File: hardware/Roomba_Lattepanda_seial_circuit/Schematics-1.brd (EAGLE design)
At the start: 32.7 x 25.4 mm, 13 parts

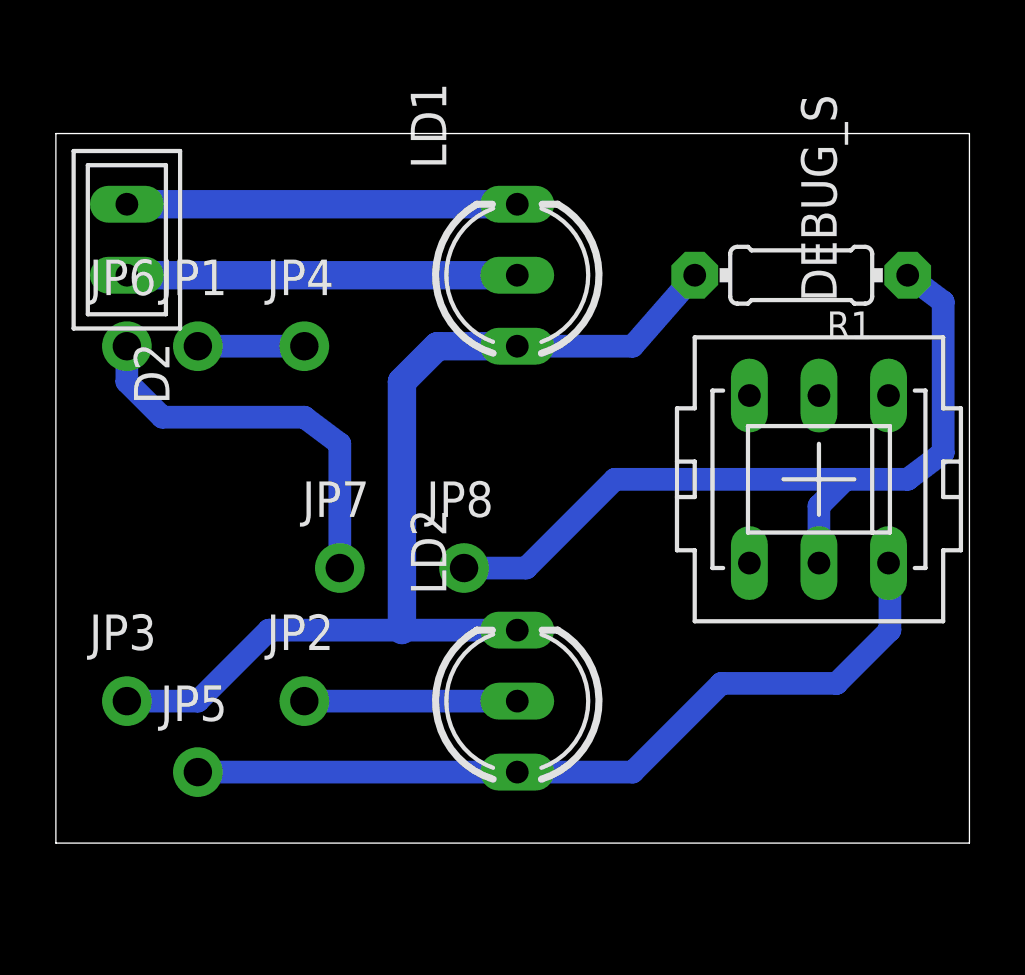
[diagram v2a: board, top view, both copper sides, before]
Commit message: add new concept art to repo + fix the style of media list + toggle augment
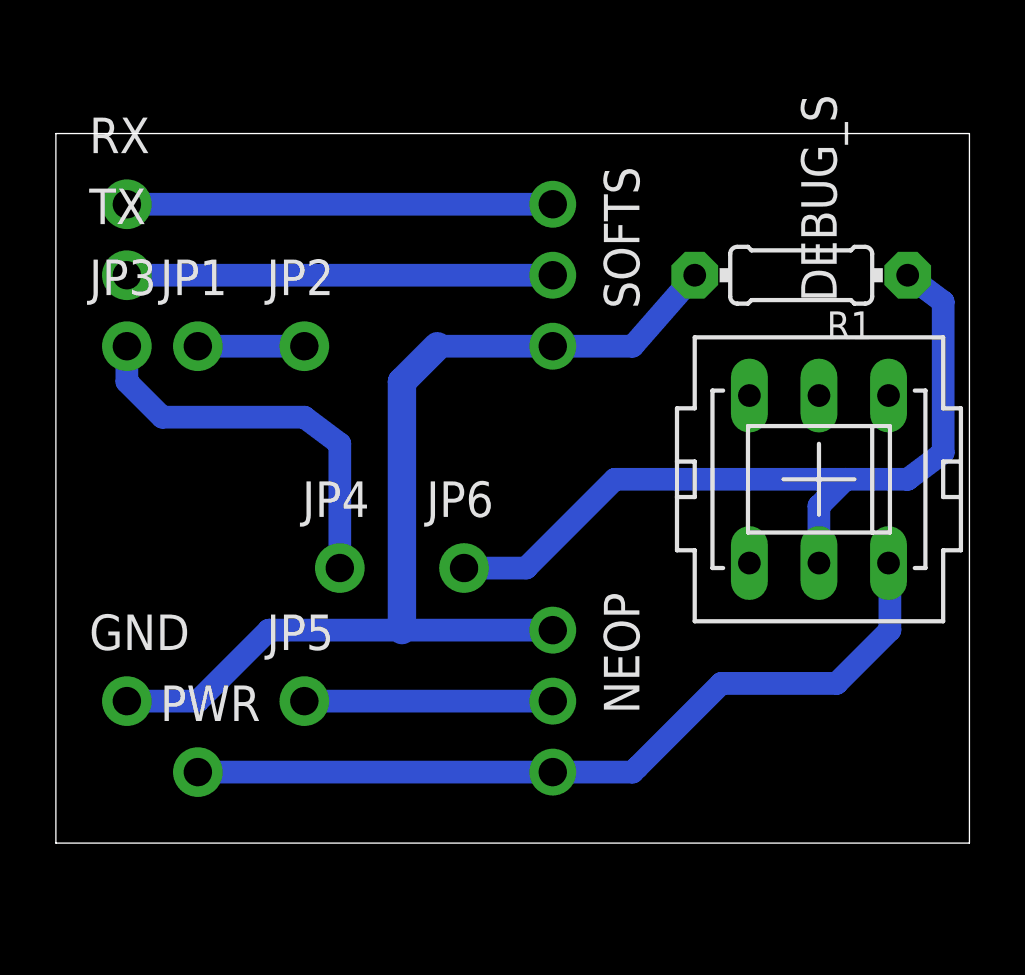
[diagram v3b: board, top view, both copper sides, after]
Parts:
- removed D2: U57X32, led:U57X32
- removed JP7, JP8: (no value), adafruit:1X01-CLEANBIG
- removed LD1, LD2: (no value), led:DUOLED-C-5MM
- added GND, PWR, RX, TX: (no value), adafruit:1X01-CLEANBIG
- added NEOP, SOFTS: (no value), adafruit:1X03-CLEANBIG
- moved JP6 14.4 mm to (14.6, 9.84)
- moved JP2 12.7 mm to (8.89, 17.8)
- moved JP3 12.7 mm to (2.54, 17.8)
- moved JP4 8.04 mm to (10.2, 9.84)
- moved JP5 4.58 mm to (8.89, 5.08)
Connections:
- net N$1: now also RX.1, SOFTS.1; no longer D2.A, LD1.AR
- net N$2: now also JP2.1; no longer JP4.1
- net N$3: now also SOFTS.2, TX.1; no longer D2.K, LD1.C
- net N$4: now also GND.1, NEOP.1, SOFTS.3; no longer JP3.1, LD1.AX, LD2.AR
- net N$5: now also NEOP.3, PWR.1; no longer JP5.1, LD2.AX
- net N$6: now also JP6.1; no longer JP8.1
- net N$7: now also JP5.1, NEOP.2; no longer JP2.1, LD2.C
- net N$8: now also JP3.1, JP4.1; no longer JP6.1, JP7.1
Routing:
- net N$7: track 7.62 -> 8.89 mm
- net N$3: track 14.0 -> 15.2 mm
- net N$1: track 14.0 -> 15.2 mm
- net N$4: track 36.1 -> 37.3 mm
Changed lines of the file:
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@@
 </autorouter>
 <elements>
-<element name="LD1" library="led" package="DUOLED-C-5MM" value="" x="16.51" y="20.32" rot="R90"/>
-<element name="D2" library="led" package="U57X32" value="U57X32" x="2.54" y="21.59" rot="R270"/>
 <element name="JP1" library="adafruit" package="1X01-CLEANBIG" value="" x="5.08" y="17.78"/>
-<element name="LD2" library="led" package="DUOLED-C-5MM" value="" x="16.51" y="5.08" rot="R90"/>
-<element name="JP2" library="adafruit" package="1X01-CLEANBIG" value="" x="8.89" y="5.08"/>
-<element name="JP4" library="adafruit" package="1X01-CLEANBIG" value="" x="8.89" y="17.78"/>
-<element name="JP3" library="adafruit" package="1X01-CLEANBIG" value="" x="2.54" y="5.08"/>
-<element name="JP5" library="adafruit" package="1X01-CLEANBIG" value="" x="5.08" y="2.54"/>
+<element name="JP5" library="adafruit" package="1X01-CLEANBIG" value="" x="8.89" y="5.08"/>
+<element name="JP2" library="adafruit" package="1X01-CLEANBIG" value="" x="8.89" y="17.78"/>
+<element name="GND" library="adafruit" package="1X01-CLEANBIG" value="" x="2.54" y="5.08"/>
+<element name="PWR" library="adafruit" package="1X01-CLEANBIG" value="" x="5.08" y="2.54"/>
 <element name="R1" library="adafruit" package="0204/7" value="" x="26.67" y="20.32" rot="R180"/>
 <element name="DEBUG_S" library="switch-misc" package="PVA2R" value="PVA2R" x="27.305" y="13.0175" rot="R90"/>
-<element name="JP6" library="adafruit" package="1X01-CLEANBIG" value="" x="2.54" y="17.78"/>
-<element name="JP7" library="adafruit" package="1X01-CLEANBIG" value="" x="10.16" y="9.8425"/>
-<element name="JP8" library="adafruit" package="1X01-CLEANBIG" value="" x="14.605" y="9.8425"/>
+<element name="JP3" library="adafruit" package="1X01-CLEANBIG" value="" x="2.54" y="17.78"/>
+<element name="JP4" library="adafruit" package="1X01-CLEANBIG" value="" x="10.16" y="9.8425"/>
+<element name="JP6" library="adafruit" package="1X01-CLEANBIG" value="" x="14.605" y="9.8425"/>
+<element name="NEOP" library="adafruit" package="1X03-CLEANBIG" value="" x="17.78" y="5.08" rot="R270"/>
+<element name="SOFTS" library="adafruit" package="1X03-CLEANBIG" value="" x="17.78" y="20.32" rot="R270"/>
+<element name="RX" library="adafruit" package="1X01-CLEANBIG" value="" x="2.54" y="22.86"/>
+<element name="TX" library="adafruit" package="1X01-CLEANBIG" value="" x="2.54" y="20.32"/>
 </elements>
 <signals>
 <signal name="N$4">
-<contactref element="LD1" pad="AX"/>
 <wire x1="12.3825" y1="7.62" x2="12.3825" y2="16.51" width="1.016" layer="16"/>
 <wire x1="12.3825" y1="16.51" x2="13.6525" y2="17.78" width="1.016" layer="16"/>
-<wire x1="13.6525" y1="17.78" x2="16.51" y2="17.78" width="1.016" layer="16"/>
-<contactref element="LD2" pad="AR"/>
-<wire x1="16.51" y1="7.62" x2="12.3825" y2="7.62" width="0.8128" layer="16"/>
 <wire x1="12.3825" y1="7.62" x2="7.62" y2="7.62" width="0.8128" layer="16"/>
 <wire x1="7.62" y1="7.62" x2="5.08" y2="5.08" width="0.8128" layer="16"/>
-<contactref element="JP3" pad="1"/>
+<contactref element="GND" pad="1"/>
 <wire x1="2.54" y1="5.08" x2="5.08" y2="5.08" width="0.8128" layer="16"/>
 <contactref element="R1" pad="2"/>
-<wire x1="16.51" y1="17.78" x2="20.6375" y2="17.78" width="0.8128" layer="16"/>
 <wire x1="20.6375" y1="17.78" x2="22.86" y2="20.32" width="0.8128" layer="16"/>
+<contactref element="SOFTS" pad="3"/>
+<contactref element="NEOP" pad="1"/>
+<wire x1="20.6375" y1="17.78" x2="18.0975" y2="17.78" width="0.8128" layer="16"/>
+<wire x1="17.78" y1="17.78" x2="13.6525" y2="17.78" width="0.8128" layer="16"/>
+<wire x1="17.78" y1="7.62" x2="12.3825" y2="7.62" width="0.8128" layer="16"/>
+<wire x1="17.78" y1="17.78" x2="18.0975" y2="17.78" width="0.8128" layer="16"/>
 </signal>
 <signal name="N$1">
-<contactref element="D2" pad="A"/>
-<contactref element="LD1" pad="AR"/>
-<wire x1="2.54" y1="22.86" x2="16.51" y2="22.86" width="1.016" layer="16"/>
+<contactref element="SOFTS" pad="1"/>
+<contactref element="RX" pad="1"/>
+<wire x1="2.54" y1="22.86" x2="17.78" y2="22.86" width="0.8128" layer="16"/>
 </signal>
 <signal name="N$3">
-<contactref element="D2" pad="K"/>
-<contactref element="LD1" pad="C"/>
-<wire x1="2.54" y1="20.32" x2="16.51" y2="20.32" width="1.016" layer="16"/>
+<contactref element="SOFTS" pad="2"/>
+<contactref element="TX" pad="1"/>
+<wire x1="2.54" y1="20.32" x2="17.78" y2="20.32" width="0.8128" layer="16"/>
 </signal>
 <signal name="N$5">
-<contactref element="LD2" pad="AX"/>
-<contactref element="JP5" pad="1"/>
-<wire x1="5.08" y1="2.54" x2="16.51" y2="2.54" width="0.8128" layer="16"/>
-<wire x1="16.51" y1="2.54" x2="20.6375" y2="2.54" width="0.8128" layer="16"/>
+<contactref element="PWR" pad="1"/>
 <contactref element="DEBUG_S" pad="3"/>
-<wire x1="20.6375" y1="2.54" x2="23.8125" y2="5.715" width="0.8128" layer="16"/>
+<wire x1="20.79625" y1="2.69875" x2="23.8125" y2="5.715" width="0.8128" layer="16"/>
 <wire x1="23.8125" y1="5.715" x2="27.94" y2="5.715" width="0.8128" layer="16"/>
 <wire x1="27.94" y1="5.715" x2="29.845" y2="7.62" width="0.8128" layer="16"/>
 <wire x1="29.845" y1="7.62" x2="29.845" y2="9.9695" width="0.8128" layer="16"/>
 <wire x1="29.845" y1="9.9695" x2="29.7942" y2="10.0203" width="0.8128" layer="16"/>
+<contactref element="NEOP" pad="3"/>
+<wire x1="5.08" y1="2.54" x2="17.78" y2="2.54" width="0.8128" layer="16"/>
+<wire x1="17.78" y1="2.54" x2="20.6375" y2="2.54" width="0.8128" layer="16"/>
+<wire x1="20.6375" y1="2.54" x2="20.79625" y2="2.69875" width="0.8128" layer="16"/>
 </signal>
 <signal name="N$2">
 <contactref element="JP1" pad="1"/>
 <wire x1="5.08" y1="17.78" x2="8.89" y2="17.78" width="0.8128" layer="16"/>
-<contactref element="JP4" pad="1"/>
+<contactref element="JP2" pad="1"/>
 </signal>
 <signal name="N$7">
-<contactref element="LD2" pad="C"/>
-<contactref element="JP2" pad="1"/>
-<wire x1="8.89" y1="5.08" x2="16.51" y2="5.08" width="0.8128" layer="16"/>
+<contactref element="JP5" pad="1"/>
+<contactref element="NEOP" pad="2"/>
+<wire x1="8.89" y1="5.08" x2="17.78" y2="5.08" width="0.8128" layer="16"/>
 </signal>
 <signal name="N$6">
@@
 <wire x1="31.75" y1="13.97" x2="31.75" y2="19.3675" width="0.8128" layer="16"/>
 <wire x1="30.48" y1="20.32" x2="31.75" y2="19.3675" width="0.8128" layer="16"/>
-<contactref element="JP8" pad="1"/>
+<contactref element="JP6" pad="1"/>
 <wire x1="14.605" y1="9.8425" x2="16.8275" y2="9.8425" width="0.8128" layer="16"/>
 <wire x1="16.8275" y1="9.8425" x2="20.0025" y2="13.0175" width="0.8128" layer="16"/>
@@
 </signal>
 <signal name="N$8">
-<contactref element="JP6" pad="1"/>
-<contactref element="JP7" pad="1"/>
+<contactref element="JP3" pad="1"/>
+<contactref element="JP4" pad="1"/>
 <wire x1="2.54" y1="17.78" x2="2.54" y2="16.51" width="0.8128" layer="16"/>
 <wire x1="2.54" y1="16.51" x2="3.81" y2="15.24" width="0.8128" layer="16"/>
